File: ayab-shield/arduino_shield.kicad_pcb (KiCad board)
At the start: 2 copper layers, 73.1 x 53.3 mm, 35 parts, among them IC1 ULN2803A, IC2 ULN2803A, IC3 MCP2300X/P, IC4 MCP2300X/P, J1 Power, J2 Digital/PWM, J3 Analog, J4 Digital/PWM, X1 KLDX-0202-AC

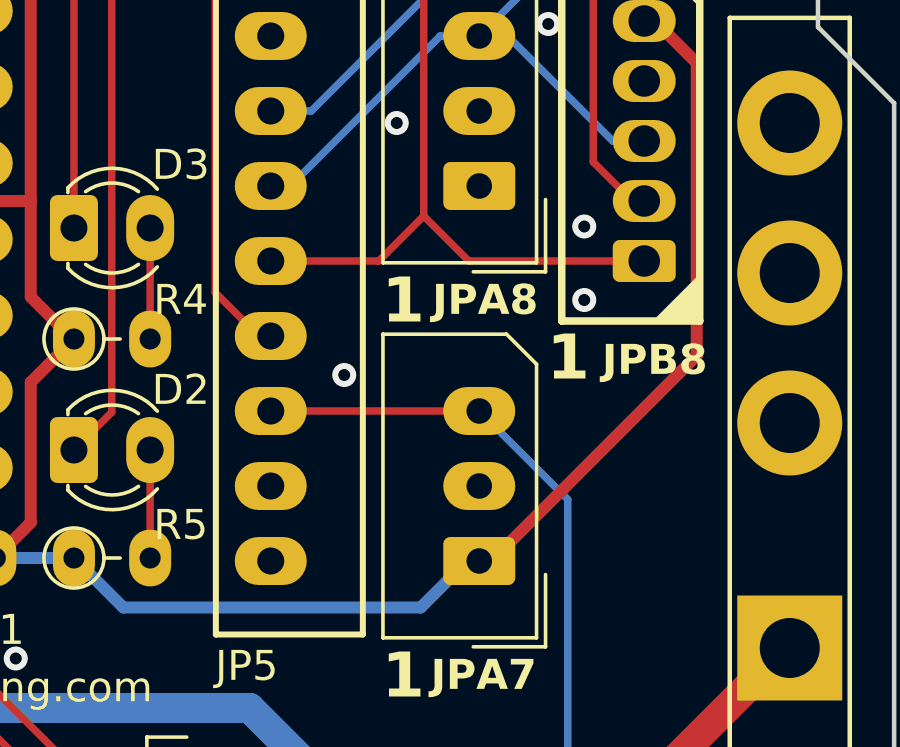
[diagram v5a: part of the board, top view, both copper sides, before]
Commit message: Fix DRC error
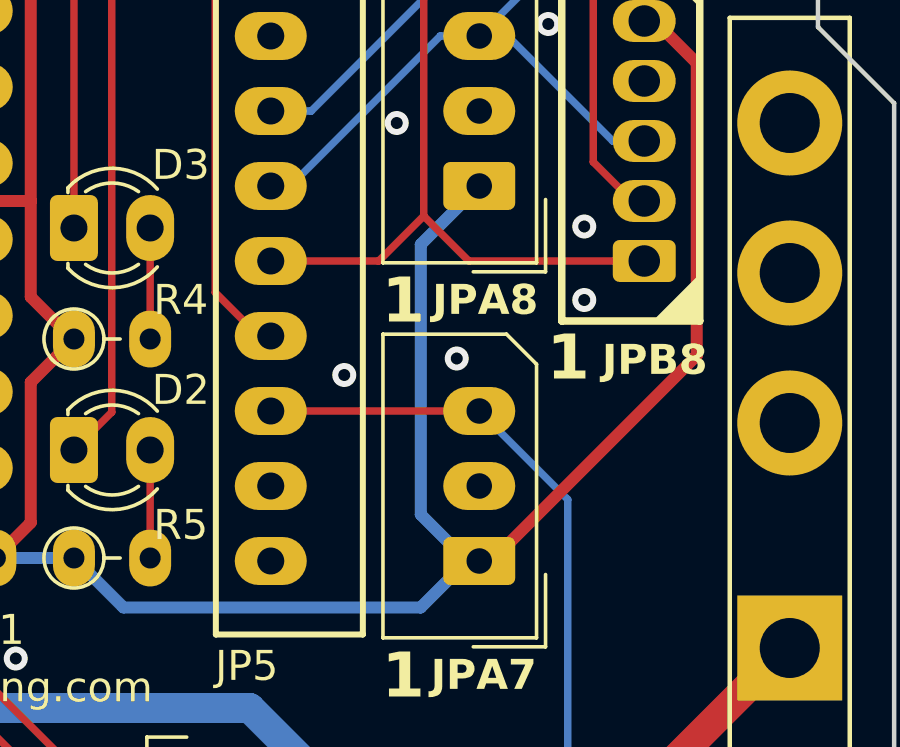
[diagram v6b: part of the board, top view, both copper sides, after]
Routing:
- net +5V: track 179.5 -> 193.4 mm
- net GND: vias 26 -> 27
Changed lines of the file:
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@@
+	)
+	(via
+		(at 168.7 100.45)
+		(size 0.8)
+		(drill 0.4)
+		(layers "F.Cu" "B.Cu")
+		(free yes)
+		(net 2)
 	)
 	(via
@@
 	)
 	(segment
+		(start 169.05 107.2)
+		(end 167.5 105.65)
+		(width 0.4)
+		(layer "B.Cu")
+		(net 3)
+	)
+	(segment
 		(start 132.44 120.66)
 		(end 131.9 120.66)
@@
 	)
 	(segment
+		(start 167.5 105.65)
+		(end 167.5 96.65)
+		(width 0.4)
+		(layer "B.Cu")
+		(net 3)
+	)
+	(segment
 		(start 139.52 107.96)
 		(end 139.96 107.96)
@@
 		(layer "B.Cu")
 		(net 3)
+	)
+	(segment
+		(start 167.5 96.65)
+		(end 169.45 94.7)
+		(width 0.4)
+		(layer "B.Cu")
+		(net 3)

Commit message: Fix bottom silkscreen
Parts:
- added JPB7: 1X3 2mm, ayab-library:CONN-TH_3P-P2.00_A2004WV-3P, F.Cu at (175.1, 105.8)
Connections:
- JPA2 pad 1: +5V -> /EOL_L
- JPA2 pad 3: /EOL_L -> +5V
- JPA7 pad 1: +5V -> GND
- JPA7 pad 2: GND -> /EOL_R
- JPA7 pad 3: /EOL_R -> +5V
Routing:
- net /910_L: track 27.0 -> 38.0 mm, vias 1 -> 0
- net GND: track 17.5 -> 19.9 mm, vias 27 -> 26
- net /EOL_R: track 37.3 -> 39.6 mm
- net +5V: track 193.4 -> 191.7 mm
- net /EOL_L: track 30.4 -> 29.2 mm

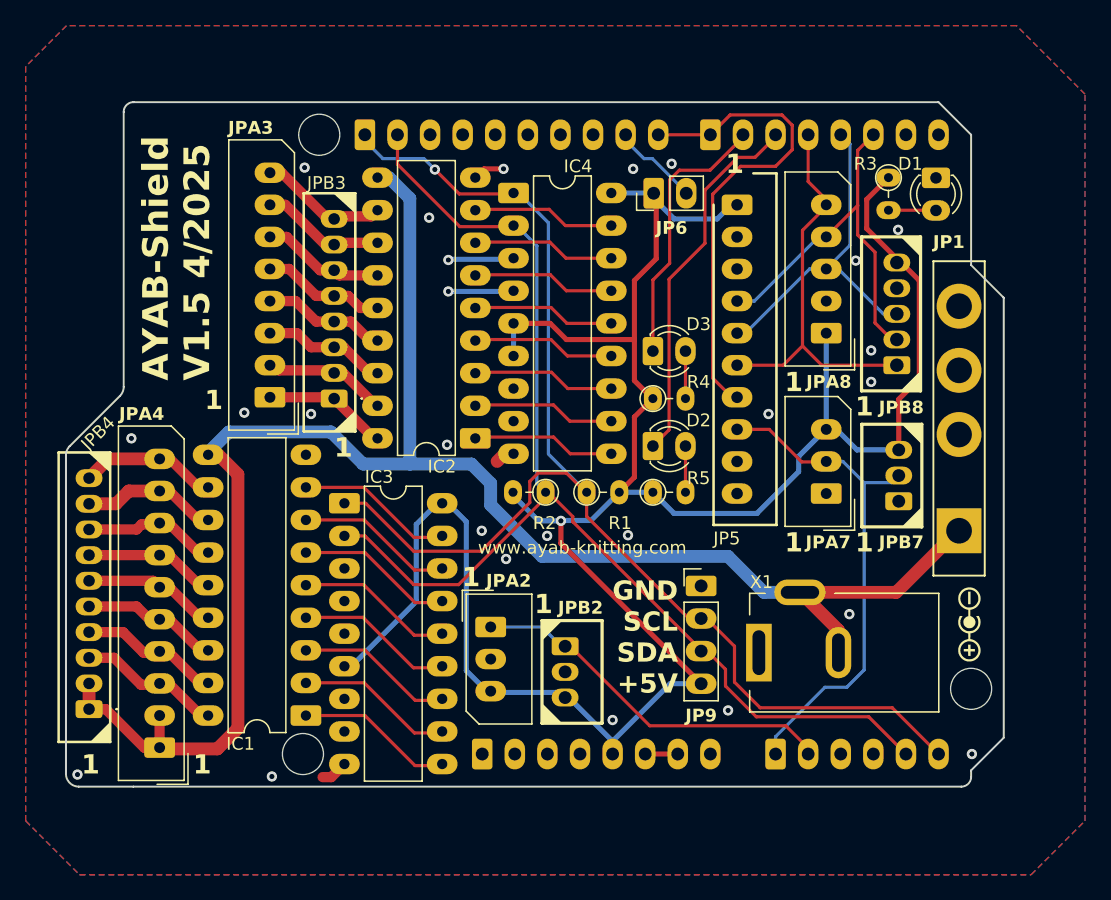
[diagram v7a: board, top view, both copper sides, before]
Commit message: Remove paste from footprints, make all 2mm pitch connectors have 1mm diameter hole
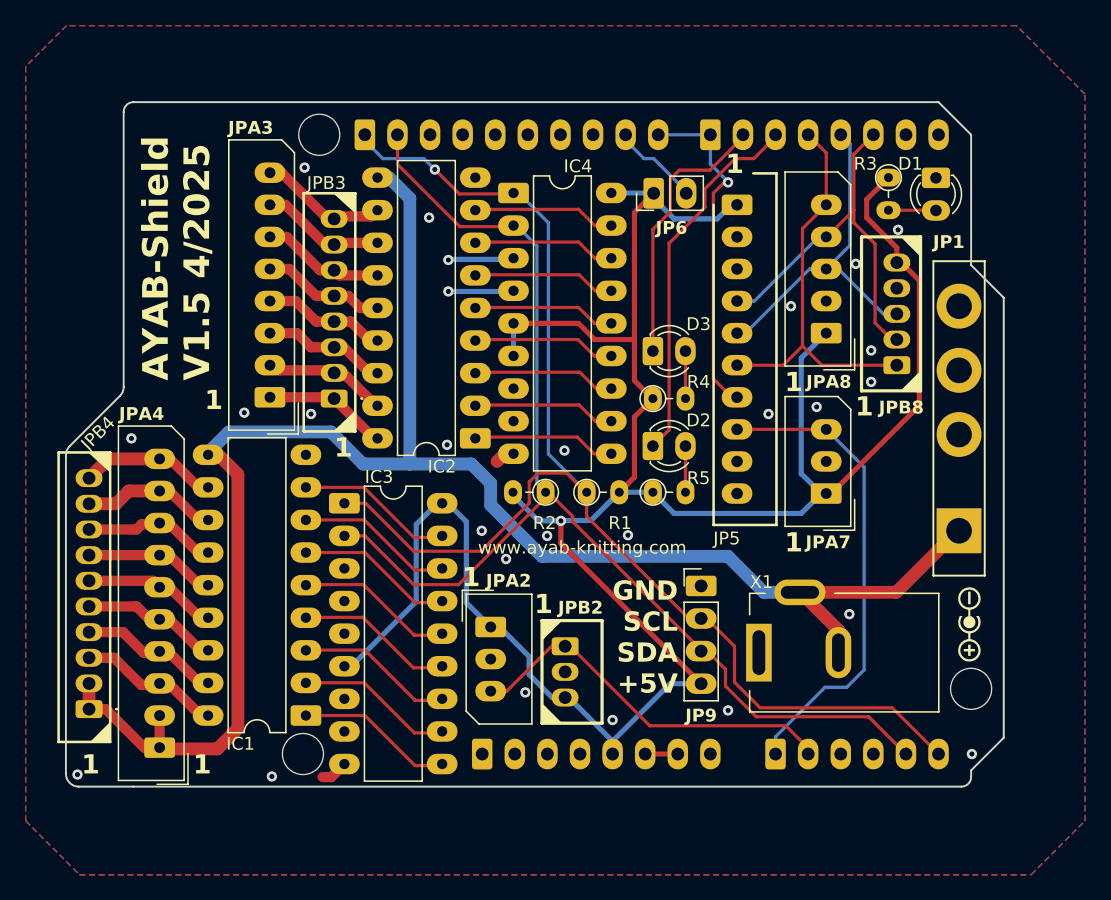
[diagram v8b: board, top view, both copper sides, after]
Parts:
- removed JPB7: 1X3 2mm, ayab-library:CONN-TH_3P-P2.00_A2004WV-3P
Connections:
- JPA2 pad 1: /EOL_L -> +5V
- JPA2 pad 3: +5V -> /EOL_L
- JPA7 pad 1: GND -> +5V
- JPA7 pad 2: /EOL_R -> GND
- JPA7 pad 3: +5V -> /EOL_R
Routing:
- net /910_L: track 38.0 -> 27.0 mm, vias 0 -> 1
- net GND: track 19.9 -> 17.5 mm, vias 26 -> 27
- net /EOL_R: track 39.6 -> 37.3 mm
- net +5V: track 191.7 -> 193.4 mm
- net /EOL_L: track 29.2 -> 30.4 mm
